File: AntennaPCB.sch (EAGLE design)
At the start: 25 parts, among them Q1 27.12MHz

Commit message: Copied the Antenna board from external circuit to create my own antenna.
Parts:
- added J1: BM02B-ACHSS-GAN-TF(LF)(SN), BM02B-ACHSS-GAN-TF_LF__SN_:BM02B-ACHSS-GAN-TF(LF)(SN)
- added R7: 0, Resistor_Capacitor:ERJ-8GEY0R00V
- added U$2: T2I-02, SeniorDesignParts:T2I-02
- C7, C8: value 1uf -> 7pF
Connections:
- removed net SCK: R4.1, U$1.D5/ADR_1/SCK/DTQR
- removed net SDA: R3.1, U$1.SDA/NSS/RX
- new net N$7: J1.SHIELD, R7.1
- net ANTC_1: now also J1.1, U$2.P$1
- net ANTC_2: now also J1.2, U$2.P$2
- net GND: now also R7.2
- net SCLK: now also R4.1, U$1.D5/ADR_1/SCK/DTQR
- net SS: now also R3.1, U$1.SDA/NSS/RX

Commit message: Created the antenna board and adjusted sizing of the board
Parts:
- removed J1: BM02B-ACHSS-GAN-TF(LF)(SN), BM02B-ACHSS-GAN-TF_LF__SN_:BM02B-ACHSS-GAN-TF(LF)(SN)
- removed R7: 0, Resistor_Capacitor:ERJ-8GEY0R00V
- removed U$2: T2I-02, SeniorDesignParts:T2I-02
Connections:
- removed net ANTC_1: J1.1, R5.1, U$2.P$1
- removed net ANTC_2: J1.2, R6.1, U$2.P$2
- removed net N$7: J1.SHIELD, R7.1
- new net ANTENNA: R5.1, R6.1
- net GND: no longer R7.2
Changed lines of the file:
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@@
 <part name="R5" library="Resistor_Capacitor" library_urn="urn:adsk.eagle:library:11396451" deviceset="ERJ-8GEY0R00V" device="" package3d_urn="urn:adsk.eagle:package:10872898/2" value="0"/>
 <part name="R6" library="Resistor_Capacitor" library_urn="urn:adsk.eagle:library:11396451" deviceset="ERJ-8GEY0R00V" device="" package3d_urn="urn:adsk.eagle:package:10872898/2" value="0"/>
-<part name="U$2" library="SeniorDesignParts" deviceset="T2I-02" device=""/>
-<part name="J1" library="BM02B-ACHSS-GAN-TF_LF__SN_" deviceset="BM02B-ACHSS-GAN-TF(LF)(SN)" device="" value=""/>
-<part name="GND13" library="supply1" library_urn="urn:adsk.eagle:library:371" deviceset="GND" device=""/>
-<part name="R7" library="Resistor_Capacitor" library_urn="urn:adsk.eagle:library:11396451" deviceset="ERJ-8GEY0R00V" device="" package3d_urn="urn:adsk.eagle:package:10872898/2" value="0"/>
 <part name="GND10" library="supply1" library_urn="urn:adsk.eagle:library:371" deviceset="GND" device=""/>
 <part name="GND11" library="supply1" library_urn="urn:adsk.eagle:library:371" deviceset="GND" device=""/>
@@
 <instance part="R5" gate="G$1" x="104.14" y="12.7" rot="R180"/>
 <instance part="R6" gate="G$1" x="104.14" y="45.72" rot="R180"/>
-<instance part="U$2" gate="G$1" x="142.24" y="45.72"/>
-<instance part="J1" gate="G$1" x="142.24" y="22.86"/>
-<instance part="GND13" gate="1" x="127" y="5.08">
-<attribute name="VALUE" x="124.46" y="2.54" size="1.778" layer="96"/>
-</instance>
-<instance part="R7" gate="G$1" x="127" y="15.24" rot="R270"/>
 <instance part="GND10" gate="1" x="63.5" y="25.4">
 <attribute name="VALUE" x="60.96" y="22.86" size="1.778" layer="96"/>
@@
 <wire x1="99.06" y1="119.38" x2="83.82" y2="119.38" width="0.1524" layer="91"/>
 <pinref part="GND3" gate="1" pin="GND"/>
-</segment>
-<segment>
-<pinref part="R7" gate="G$1" pin="2"/>
-<pinref part="GND13" gate="1" pin="GND"/>
-<wire x1="127" y1="10.16" x2="127" y2="7.62" width="0.1524" layer="91"/>
 </segment>
 <segment>
@@
 </segment>
 </net>
-<net name="ANTC_1" class="0">
-<segment>
+<net name="ANTENNA" class="0">
+<segment>
+<pinref part="R6" gate="G$1" pin="1"/>
 <pinref part="R5" gate="G$1" pin="1"/>
-<wire x1="109.22" y1="12.7" x2="114.3" y2="12.7" width="0.1524" layer="91"/>
-<label x="114.3" y="12.7" size="1.778" layer="95" rot="R90"/>
-</segment>
-<segment>
-<pinref part="U$2" gate="G$1" pin="P$1"/>
-<wire x1="137.16" y1="43.18" x2="132.08" y2="43.18" width="0.1524" layer="91"/>
-<label x="124.46" y="43.18" size="1.778" layer="95"/>
-</segment>
-<segment>
-<pinref part="J1" gate="G$1" pin="1"/>
-<wire x1="132.08" y1="27.94" x2="127" y2="27.94" width="0.1524" layer="91"/>
-<label x="121.92" y="30.48" size="1.778" layer="95"/>
-</segment>
-</net>
-<net name="ANTC_2" class="0">
-<segment>
-<pinref part="R6" gate="G$1" pin="1"/>
-<wire x1="109.22" y1="45.72" x2="114.3" y2="45.72" width="0.1524" layer="91"/>
-<label x="114.3" y="45.72" size="1.778" layer="95" rot="R90"/>
-</segment>
-<segment>
-<pinref part="U$2" gate="G$1" pin="P$2"/>
-<wire x1="137.16" y1="40.64" x2="132.08" y2="40.64" width="0.1524" layer="91"/>
-<label x="124.46" y="40.64" size="1.778" layer="95"/>
-</segment>
-<segment>
-<pinref part="J1" gate="G$1" pin="2"/>
-<wire x1="132.08" y1="25.4" x2="127" y2="25.4" width="0.1524" layer="91"/>
-<label x="121.92" y="22.86" size="1.778" layer="95"/>
-</segment>
-</net>
-<net name="N$7" class="0">
-<segment>
-<pinref part="J1" gate="G$1" pin="SHIELD"/>
-<wire x1="132.08" y1="20.32" x2="127" y2="20.32" width="0.1524" layer="91"/>
-<pinref part="R7" gate="G$1" pin="1"/>
-</segment>
-</net>
+<wire x1="109.22" y1="45.72" x2="109.22" y2="12.7" width="0.1524" layer="91"/>
+<label x="110" y="29" size="1.778" layer="95"/>
+</segment>
+</net>

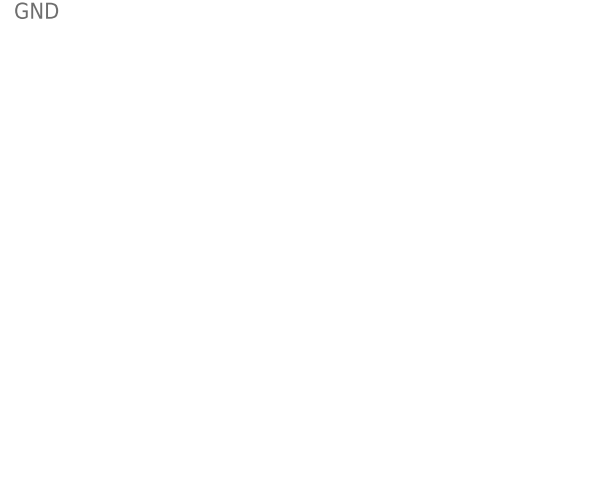
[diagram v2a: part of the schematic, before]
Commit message: Put stand-offs on the board
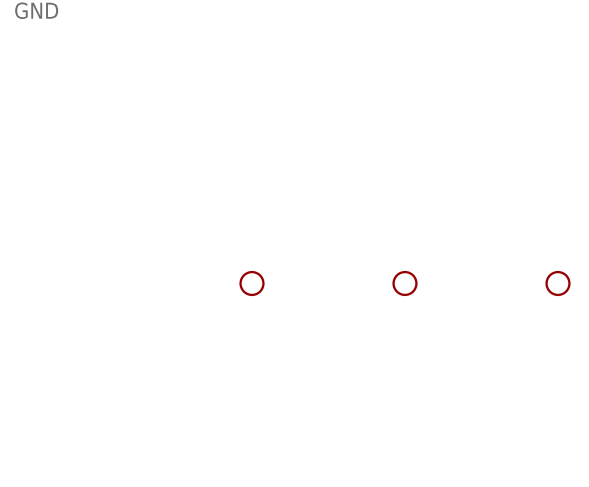
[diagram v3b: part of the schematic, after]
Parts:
- added H1, H2, H3: STAND-OFF, SparkFun-Hardware:STAND-OFF
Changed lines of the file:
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@@
 <part name="GND10" library="supply1" library_urn="urn:adsk.eagle:library:371" deviceset="GND" device=""/>
 <part name="GND11" library="supply1" library_urn="urn:adsk.eagle:library:371" deviceset="GND" device=""/>
+<part name="H1" library="SparkFun-Hardware" library_urn="urn:adsk.eagle:library:519" deviceset="STAND-OFF" device="" package3d_urn="urn:adsk.eagle:package:38630/1"/>
+<part name="H2" library="SparkFun-Hardware" library_urn="urn:adsk.eagle:library:519" deviceset="STAND-OFF" device="" package3d_urn="urn:adsk.eagle:package:38630/1"/>
+<part name="H3" library="SparkFun-Hardware" library_urn="urn:adsk.eagle:library:519" deviceset="STAND-OFF" device="" package3d_urn="urn:adsk.eagle:package:38630/1"/>
 </parts>
 <sheets>
@@
 <attribute name="VALUE" x="93.98" y="22.86" size="1.778" layer="96"/>
 </instance>
+<instance part="H1" gate="G$1" x="189" y="29"/>
+<instance part="H2" gate="G$1" x="206" y="29"/>
+<instance part="H3" gate="G$1" x="223" y="29"/>
 </instances>
 <busses>
